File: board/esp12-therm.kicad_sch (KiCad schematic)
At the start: 25 parts, among them J1 BATT, J2 I2C, J4 1W, Q1 PMF170XP, U1 TP4056_board, U2 ESP-12E, U3 TLV75533PDBV

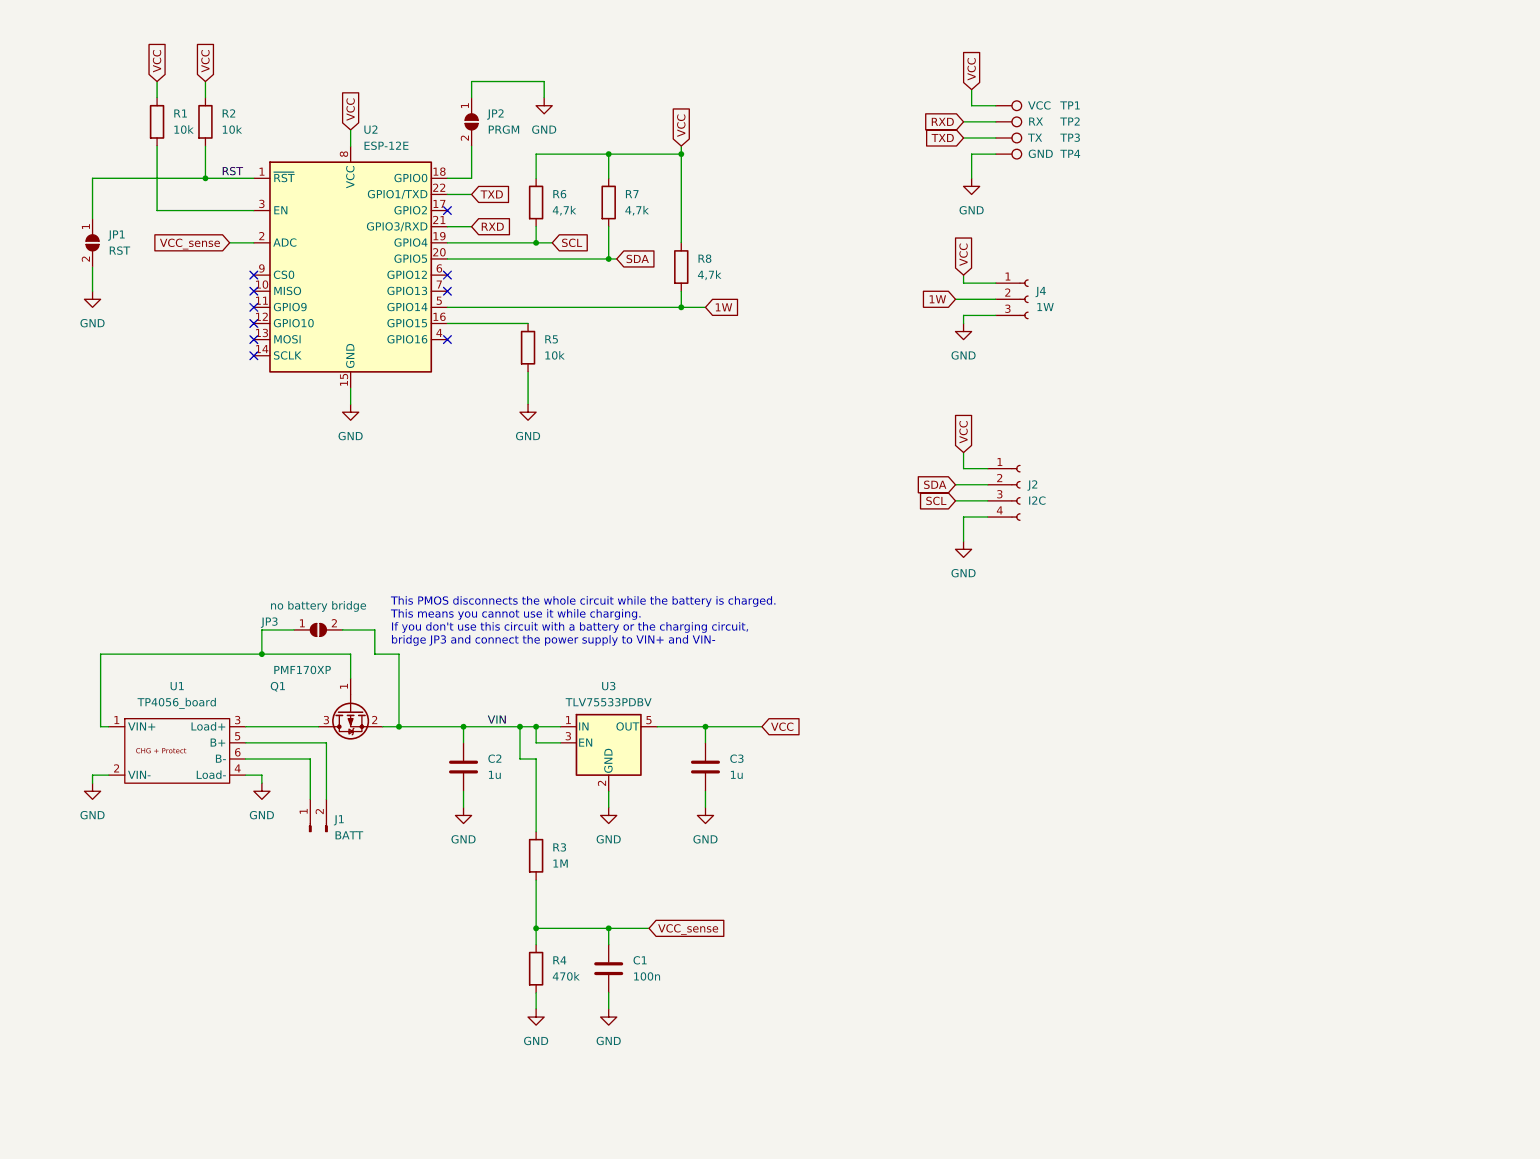
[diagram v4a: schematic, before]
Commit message: Redesign to make it a fully breakout board: * Add pads for all pins * shrink board ad far as possible * place pull up resistors close to each other at the back * replace nmos with a schottky diode
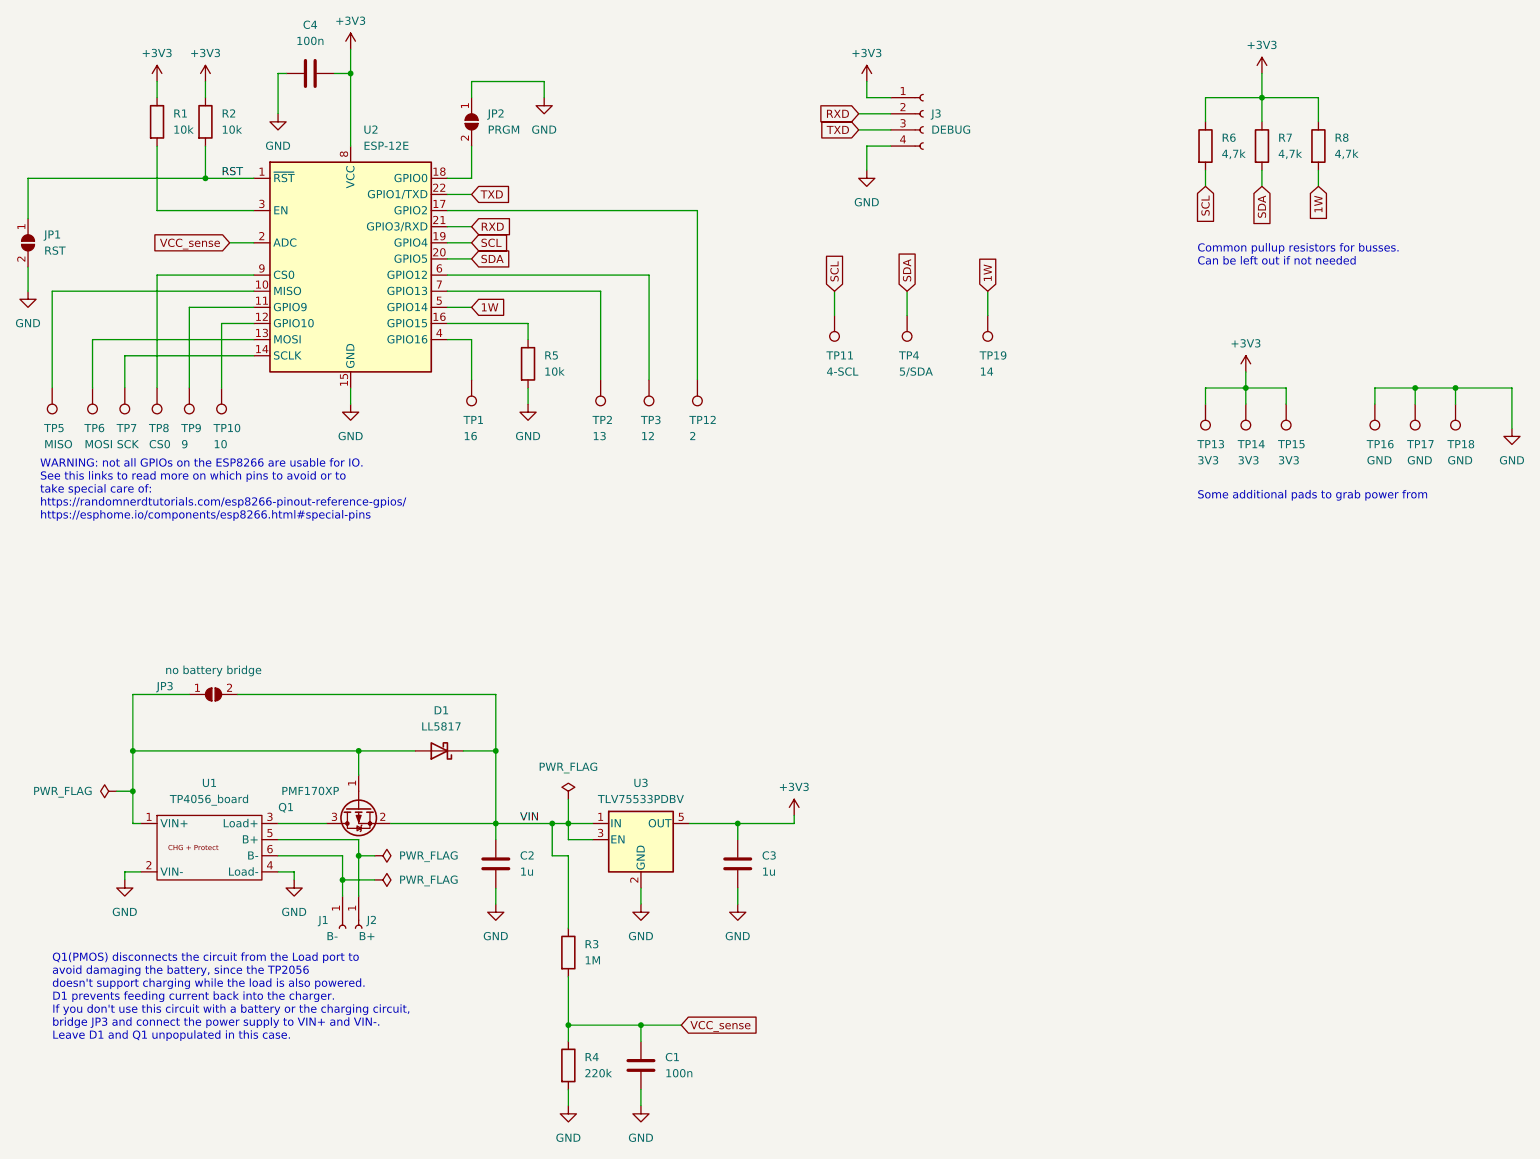
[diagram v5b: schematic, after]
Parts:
- removed J1: BATT, Connector_Molex:Molex_PicoBlade_53047-0210_1x02_P1.25mm_Vertical, symbol Connector:Conn_01x02_Male
- removed J2: I2C, Connector_PinHeader_1.27mm:PinHeader_1x04_P1.27mm_Vertical, symbol Connector:Conn_01x04_Female
- removed J4: 1W, Connector_PinHeader_1.27mm:PinHeader_1x03_P1.27mm_Vertical, symbol Connector:Conn_01x03_Female
- added C4: 100n, Capacitor_SMD:C_0805_2012Metric_Pad1.18x1.45mm_HandSolder, symbol Device:C
- added D1: LL5817, Diode_SMD:D_SOD-123, symbol Device:D_Schottky
- added J1: B-, TestPoint:TestPoint_Pad_3.0x3.0mm, symbol Connector:Conn_01x01_Socket
- added J2: B+, TestPoint:TestPoint_Pad_3.0x3.0mm, symbol Connector:Conn_01x01_Socket
- added J3: DEBUG, Connector_PinSocket_2.54mm:PinSocket_1x04_P2.54mm_Vertical, symbol Connector:Conn_01x04_Socket
- added TP10: 10, TestPoint:TestPoint_Pad_1.5x1.5mm, symbol Connector:TestPoint
- added TP11: 4-SCL, TestPoint:TestPoint_Pad_1.5x1.5mm, symbol Connector:TestPoint
- added TP12: 2, TestPoint:TestPoint_Pad_1.5x1.5mm, symbol Connector:TestPoint
- added TP13, TP14, TP15: 3V3, TestPoint:TestPoint_Pad_1.5x1.5mm, symbol Connector:TestPoint
- added TP16, TP17, TP18: GND, TestPoint:TestPoint_Pad_1.5x1.5mm, symbol Connector:TestPoint
- added TP19: 14, TestPoint:TestPoint_Pad_1.5x1.5mm, symbol Connector:TestPoint
- added TP5: MISO, TestPoint:TestPoint_Pad_1.5x1.5mm, symbol Connector:TestPoint
- added TP6: MOSI, TestPoint:TestPoint_Pad_1.5x1.5mm, symbol Connector:TestPoint
- added TP7: SCK, TestPoint:TestPoint_Pad_1.5x1.5mm, symbol Connector:TestPoint
- added TP8: CS0, TestPoint:TestPoint_Pad_1.5x1.5mm, symbol Connector:TestPoint
- added TP9: 9, TestPoint:TestPoint_Pad_1.5x1.5mm, symbol Connector:TestPoint
- R4: value 470k -> 220k
- TP1: value VCC -> 16; footprint TestPoint:TestPoint_Pad_2.5x2.5mm -> TestPoint:TestPoint_Pad_1.5x1.5mm
- TP2: value RX -> 13; footprint TestPoint:TestPoint_Pad_2.5x2.5mm -> TestPoint:TestPoint_Pad_1.5x1.5mm
- TP3: value TX -> 12; footprint TestPoint:TestPoint_Pad_2.5x2.5mm -> TestPoint:TestPoint_Pad_1.5x1.5mm
- TP4: value GND -> 5/SDA; footprint TestPoint:TestPoint_Pad_2.5x2.5mm -> TestPoint:TestPoint_Pad_1.5x1.5mm
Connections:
- net 1W: now also TP19.1
- net GND: now also C4.1, J3.4 (Pin_4), TP16.1, TP17.1, TP18.1; no longer TP4.1
- net RXD: now also J3.2 (Pin_2); no longer TP2.1
- net SCL: now also TP11.1
- net SDA: now also TP4.1
- net TXD: now also J3.3 (Pin_3); no longer TP3.1
- net VIN: now also D1.1 (K)
- net at U1.6 (B-): now also J1.1 (Pin_1)
- net at U1.5 (B+): now also J2.1 (Pin_1)
- net at U2.10 (MISO): now also TP5.1
- net at U2.11 (GPIO9): now also TP9.1
- net at U2.12 (GPIO10): now also TP10.1
- net at U2.13 (MOSI): now also TP6.1
- net at U2.14 (SCLK): now also TP7.1
- net at U2.17 (GPIO2): now also TP12.1
- net at U2.4 (GPIO16): now also TP1.1
- net at U2.6 (GPIO12): now also TP3.1
- net at U2.7 (GPIO13): now also TP2.1
- net at U2.9 (CS0): now also TP8.1
- net at JP3.1 (A), Q1.1 (G), U1.1 (VIN+): now also D1.2 (A)
- net VCC renamed +3V3
- net +3V3: now also C4.2, J3.1 (Pin_1), TP13.1, TP14.1, TP15.1; no longer TP1.1
- no-connect marks 10 -> 0
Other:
- note added: "Common pullup resistors for busses. Can be left out if not needed"
- note added: "Q1(PMOS) disconnects the circuit from the Load port to avoid damaging the battery, since the TP2056 doesn't support charging while the load is also powered. D1 prevents feeding current back into the charger. If you don't use this circuit with a battery or the charging circuit, bridge JP3 and connect the power supply to VIN+ and VIN-. Leave D1 and Q1 unpopulated in this case."
- note added: "Some additional pads to grab power from"
- note added: "WARNING: not all GPIOs on the ESP8266 are usable for IO. See this links to read more on which pins to avoid or to take special care of: https://randomnerdtutorials.com/esp8266-pinout-reference-gpios/ https://esphome.io/components/esp8266.html#special-pins"
- note removed: "This PMOS disconnects the whole circuit while the battery is charged. This means you cannot use it while charging. If you don't use this circuit with a battery or the charging circuit, bridge JP3 and connect the power supply to VIN+ and VIN-"
- moved on the sheet: C1, C2, C3, JP1, JP3, Q1, R3, R4, R5, R6, R7, R8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
